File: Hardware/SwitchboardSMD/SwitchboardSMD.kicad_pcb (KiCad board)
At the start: 2 copper layers, 70 x 40 mm, 40 parts, among them J2 S88_In_Plug, J4 S88_Out_Plug, Q1 BC237, SW1 SW_Push, SW2 SW_Push, SW3 SW_Push, SW4 SW_Push, SW5 SW_Push, SW6 SW_Push, SW7 SW_Push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

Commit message: Updates projects for manufacturing
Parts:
- moved C1 6.98 mm to (27.3, 24.1), turned to 0 degrees
- moved C4 3.79 mm to (47.6, 55.9), turned to 180 degrees
- moved C2 2.16 mm to (29.8, 55.9), turned to 180 degrees
- moved H3 0.24 mm to (87.0, 23.0)
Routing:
- net Net-(C1-Pad1): track 31.2 -> 36.0 mm
- net Net-(C2-Pad1): track 31.3 -> 29.4 mm
- net Net-(C3-Pad1): track 23.4 -> 24.3 mm
- net /DATA_IN: track 45.1 -> 45.9 mm
- net Net-(C4-Pad1): track 22.3 -> 21.6 mm
- net Net-(C5-Pad1): track 23.7 -> 22.9 mm
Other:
- outline, holes or cut-outs redrawn
- board text added: "DATA GND CLK LD RES VCC"
- board text added: "In"
- board text added: "Out"
- board text added: "RR32Can"
- board text added: "Switchboard v1.0"

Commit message: Fixed IC footprints
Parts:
- U1, U2, U3: footprint Package_SO:SOP-16_4.55x10.3mm_P1.27mm -> Package_SO:SOIC-16_3.9x9.9mm_P1.27mm
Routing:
- net Net-(U2-Pad13): track 23.5 -> 26.2 mm
- net VCC: track 174.8 -> 177.0 mm
- net Net-(U2-Pad10): track 14.2 -> 16.4 mm
- net /DATA_IN: track 45.9 -> 47.8 mm
- net /LOAD: track 67.8 -> 69.5 mm
- net Net-(U1-Pad9): track 23.9 -> 25.1 mm
- net Net-(U1-Pad1): track 17.3 -> 18.4 mm
- net Net-(U1-Pad10): track 24.6 -> 25.6 mm
- net /RESET_LOCAL: track 97.7 -> 98.6 mm
- net /CLOCK: track 71.4 -> 70.6 mm
- net Net-(U2-Pad1): track 21.7 -> 22.5 mm, vias 1 -> 0
- net Net-(U1-Pad13): track 21.4 -> 22.2 mm
- net Net-(R9-Pad1): track 2.73 -> 3.51 mm
- net Net-(R8-Pad1): track 2.72 -> 3.50 mm
- net Net-(R7-Pad1): track 2.73 -> 3.51 mm
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
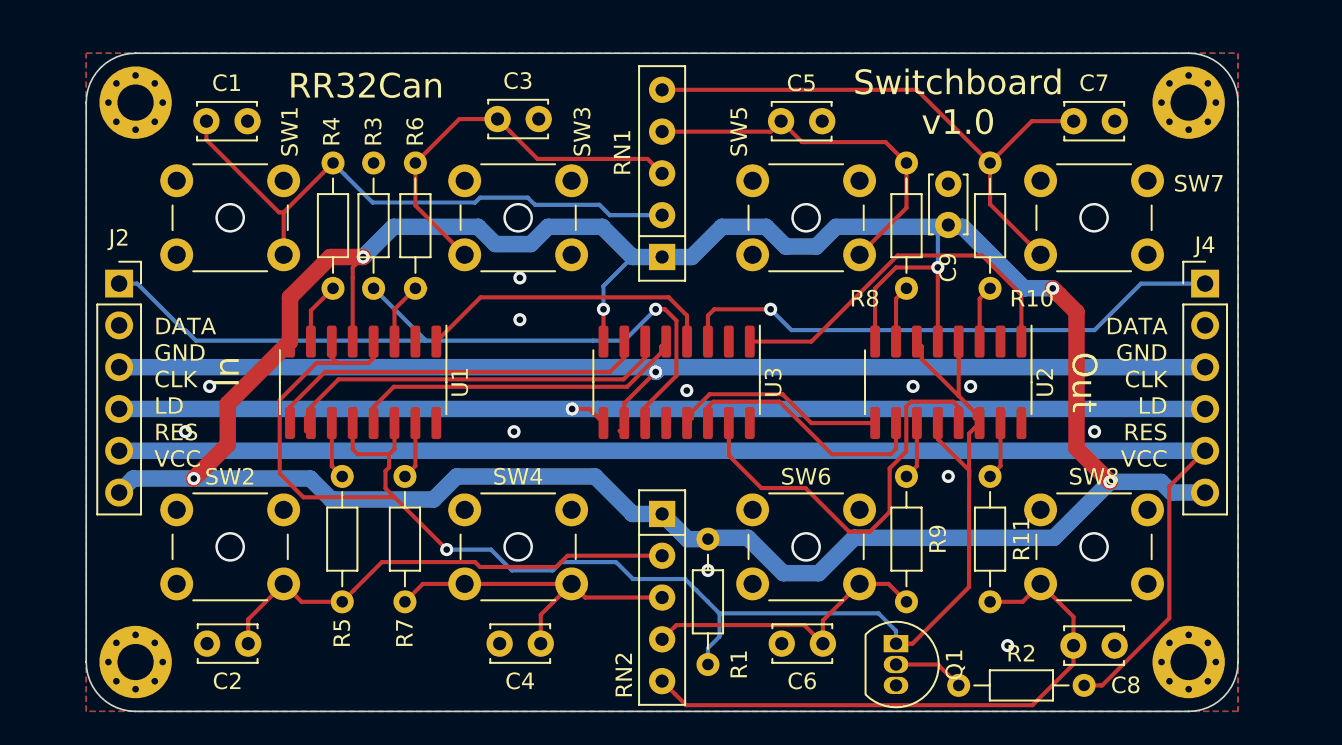
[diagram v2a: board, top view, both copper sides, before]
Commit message: Fixed inverted power connections for shift register
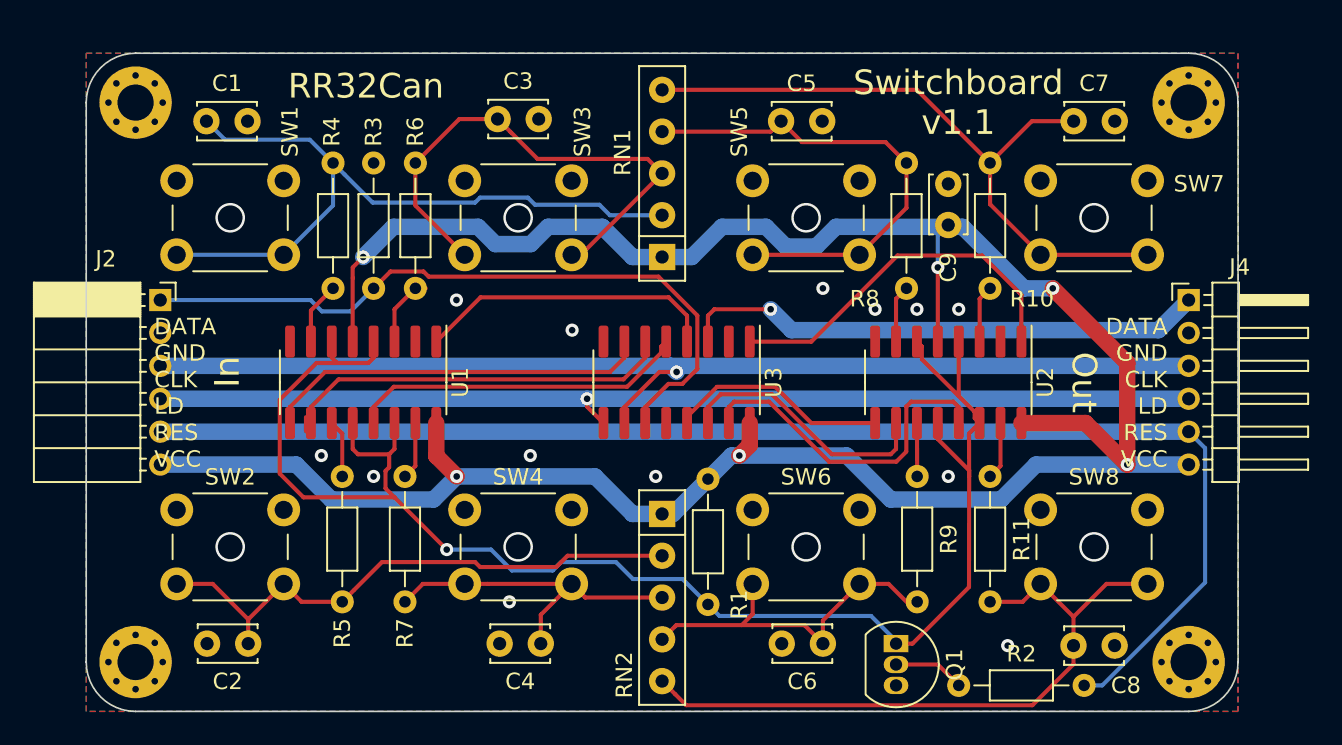
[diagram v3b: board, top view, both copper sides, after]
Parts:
- J2: footprint Connector_PinSocket_2.54mm:PinSocket_1x06_P2.54mm_Vertical -> Connector_PinSocket_2.00mm:PinSocket_1x06_P2.00mm_Horizontal
- J4: footprint Connector_PinHeader_2.54mm:PinHeader_1x06_P2.54mm_Vertical -> Connector_PinHeader_2.00mm:PinHeader_1x06_P2.00mm_Horizontal
- moved R1 3.65 mm to (57.8, 53.5)
- moved J2 2.69 mm to (24.5, 35.0)
- moved J4 1.41 mm to (87.0, 35.0)
- moved R9 0.65 mm to (70.5, 45.7)
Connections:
- U1 pad 16: GND -> VCC
- U1 pad 8: VCC -> GND
- U2 pad 16: GND -> VCC
- U2 pad 8: VCC -> GND
- U3 pad 16: GND -> VCC
- U3 pad 8: VCC -> GND
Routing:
- net VCC: track 177.0 -> 153.9 mm
- net Net-(C1-Pad1): track 36.0 -> 43.6 mm
- net Net-(C3-Pad1): track 24.3 -> 31.8 mm
- net Net-(C7-Pad1): track 34.8 -> 41.3 mm
- net Net-(C5-Pad1): track 22.9 -> 29.4 mm
- net Net-(C8-Pad1): track 35.9 -> 41.2 mm
- net Net-(C2-Pad1): track 29.4 -> 34.6 mm
- net Net-(U2-Pad13): track 26.2 -> 21.6 mm
- net /DATA_IN: track 47.8 -> 43.4 mm, vias 1 -> 0
- net /LOAD: track 69.5 -> 65.6 mm
- net /RESET_LOCAL: track 98.6 -> 94.9 mm
- net Net-(C6-Pad1): track 18.4 -> 21.2 mm
- net /CLOCK: track 70.6 -> 68.1 mm
- net /RESET: track 84.0 -> 82.0 mm
- net /DATA_OUT: track 33.6 -> 32.2 mm
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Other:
- net class Power added: clearance 0.2, trace_width 1, via_dia 0.8, via_drill 0.4
- board text added: "Switchboard v1.1"
- board text removed: "Switchboard v1.0"
